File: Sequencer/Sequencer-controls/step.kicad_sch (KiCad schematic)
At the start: 5 parts, among them SW11 SW_SPDT

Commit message: just playing around
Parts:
- renumbered D21 to D30, D22 to D31, RV_COARSE10 to RV_COARSE16, RV_FINE10 to RV_FINE16, SW11 to SW19

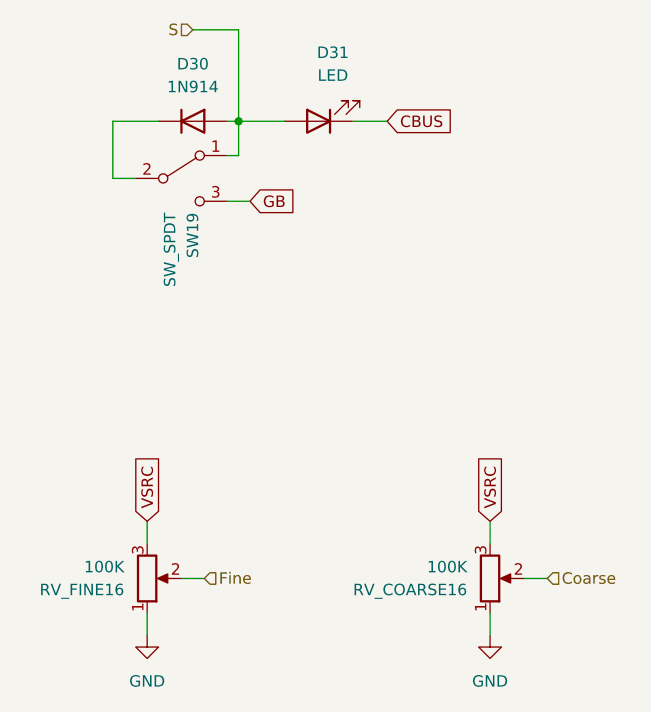
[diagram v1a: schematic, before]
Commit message: adding connectors to sequencer
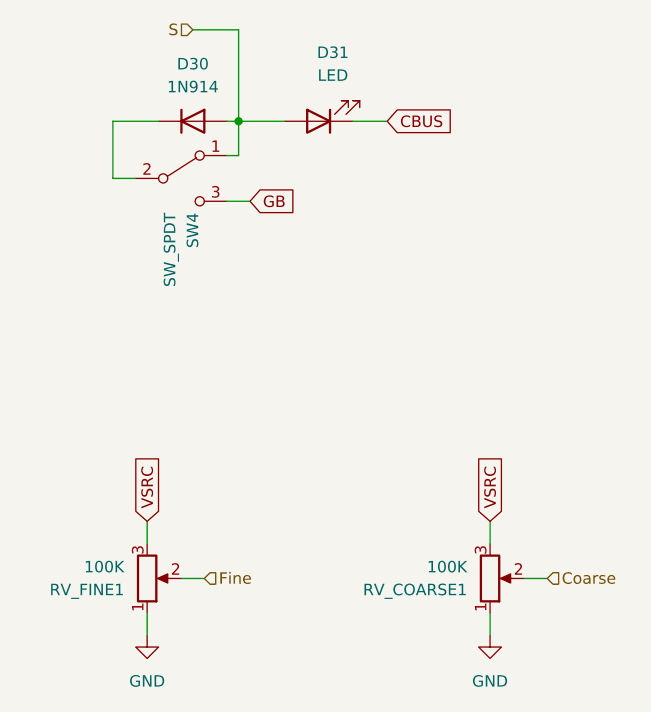
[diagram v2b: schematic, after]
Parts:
- renumbered RV_COARSE16 to RV_COARSE1, RV_FINE16 to RV_FINE1, SW19 to SW4

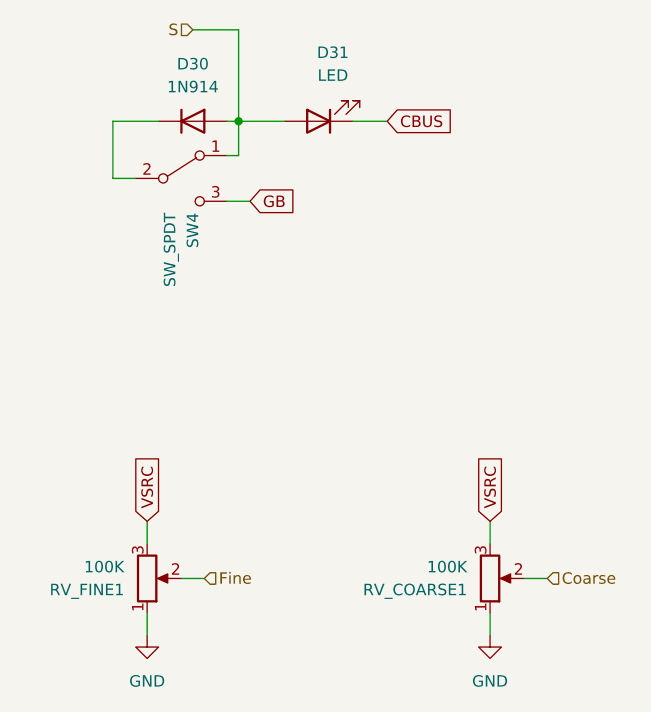
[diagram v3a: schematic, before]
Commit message: moved to 4 layers
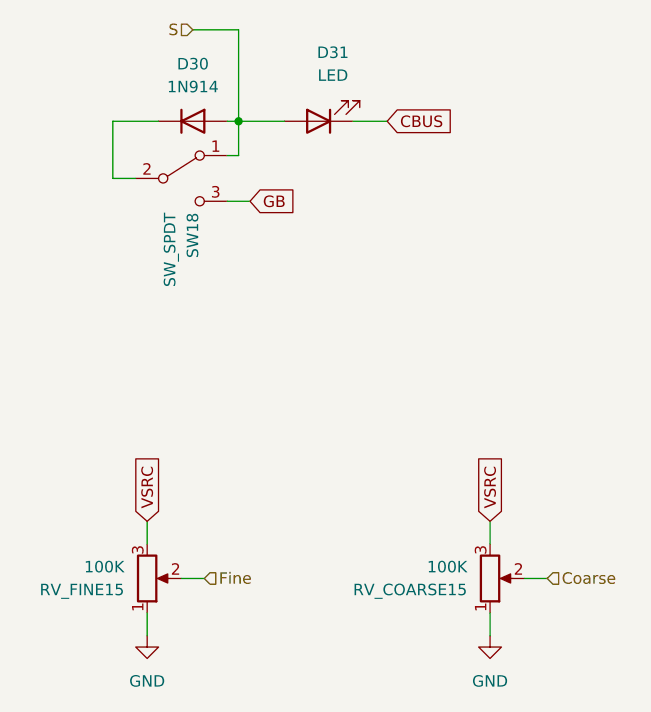
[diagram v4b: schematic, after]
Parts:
- renumbered RV_COARSE1 to RV_COARSE15, RV_FINE1 to RV_FINE15, SW4 to SW18

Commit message: misc
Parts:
- RV_COARSE1: renamed from RV_COARSE15; symbol Device:R_Potentiometer -> Device:R_Potentiometer_MountingPin
- RV_FINE1: renamed from RV_FINE15; symbol Device:R_Potentiometer -> Device:R_Potentiometer_MountingPin
- renumbered SW18 to SW4
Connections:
- net GND: now also RV_COARSE1.MP (MountPin), RV_FINE1.MP (MountPin)

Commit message: Sequencer control - minor
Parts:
- renumbered RV_COARSE1 to RV_COARSE15, RV_FINE1 to RV_FINE15, SW4 to SW18

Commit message: Sequencer - misc
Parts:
- renumbered RV_COARSE15 to RV_COARSE16, RV_FINE15 to RV_FINE16, SW18 to SW19
